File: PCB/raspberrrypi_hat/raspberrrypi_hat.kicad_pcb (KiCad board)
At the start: 4 copper layers, 65 x 56 mm, 18 parts, among them J3 40HAT, J6 CONN_02X02, J9 CONN_01X02, Q1 DMG2305UX, Q2 DMMT5401, U2 CAT24C32

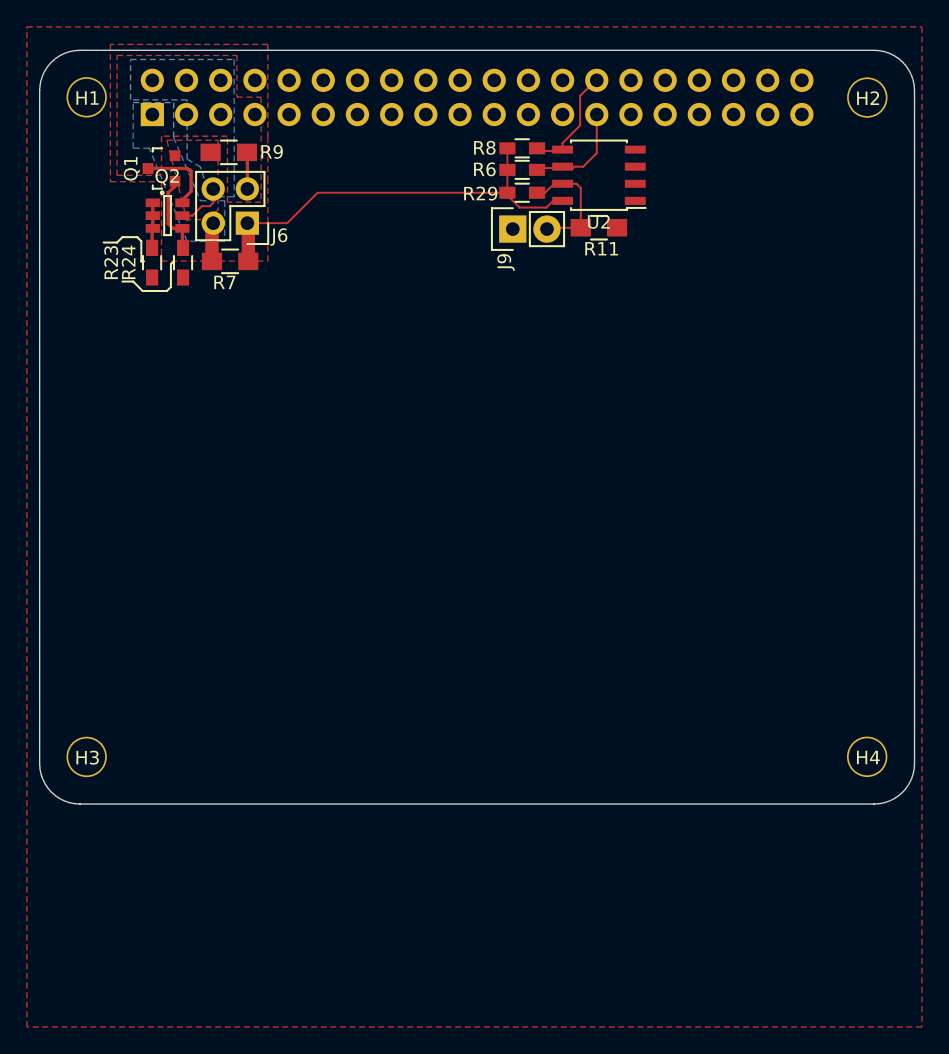
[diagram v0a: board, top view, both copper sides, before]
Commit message: Change Pi HAT footprints to SMD 1206_HandSoldering
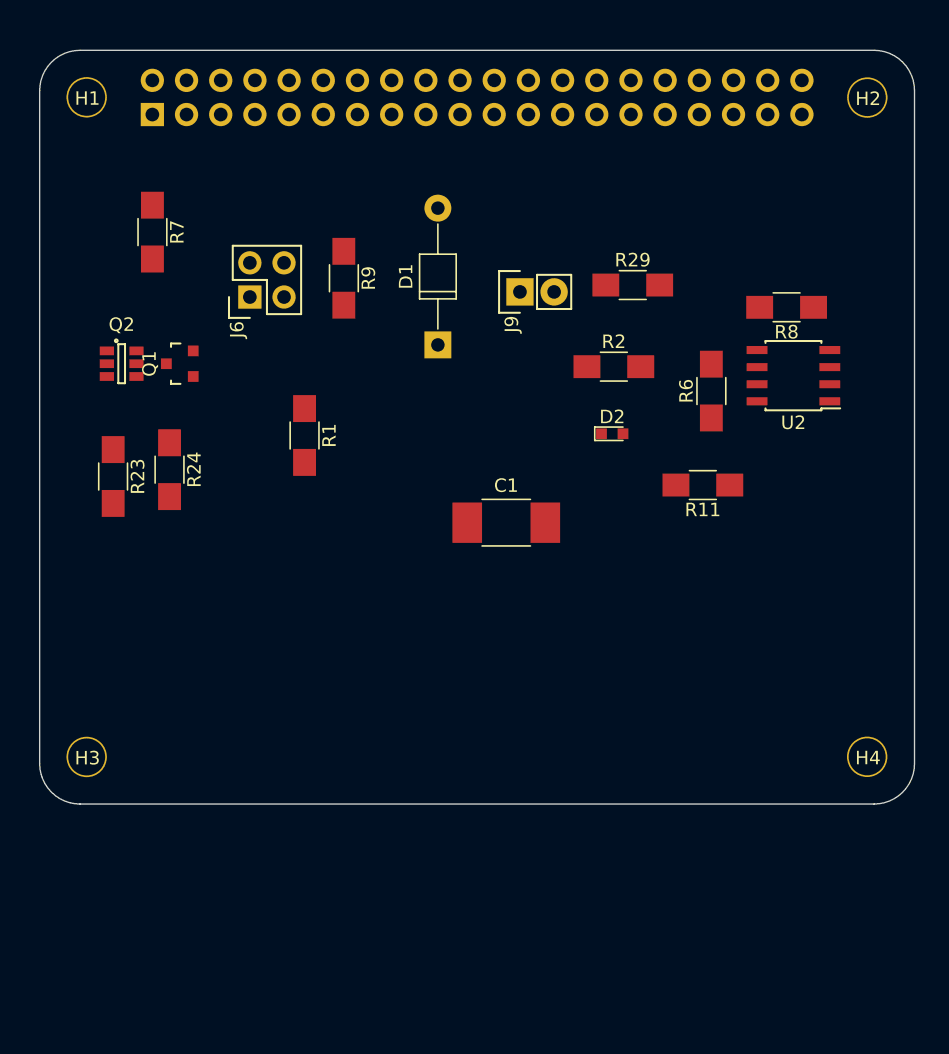
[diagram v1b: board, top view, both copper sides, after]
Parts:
- added C1: CP, Capacitors_SMD:C_1812_HandSoldering, F.Cu at (113.2, 95.9)
- added D1: D, Diodes_ThroughHole:D_T-1_P10.16mm_Horizontal, F.Cu at (108.1, 82.7)
- added D2: LED, LEDs:LED_0603, F.Cu at (121.1, 89.3)
- added R1: R, Resistors_SMD:R_1206_HandSoldering, F.Cu at (98.2, 89.4)
- added R2: R, Resistors_SMD:R_1206_HandSoldering, F.Cu at (121.2, 84.3)
- R11, R7, R9: footprint Resistors_SMD:R_0805_HandSoldering -> Resistors_SMD:R_1206_HandSoldering
- R23, R24, R29, R6, R8: footprint Resistors_SMD:R_0603_HandSoldering -> Resistors_SMD:R_1206_HandSoldering
- moved R8 22.9 mm to (134.0, 79.9), turned to 180 degrees
- moved R6 21.6 mm to (128.5, 86.1), turned to 90 degrees
- moved U2 20.7 mm to (134.6, 85.0)
- moved R11 20.6 mm to (127.8, 93.1), turned to 180 degrees
- moved R23 16.1 mm to (84.0, 92.5)
- moved R24 15.4 mm to (88.2, 92.0)
- moved Q1 14.6 mm to (89.0, 84.1)
- moved R9 12.7 mm to (101.1, 77.8), turned to 270 degrees
- moved Q2 11.5 mm to (84.6, 84.1)
- moved R29 10.7 mm to (122.6, 78.3)
- moved R7 6.17 mm to (86.9, 74.3), turned to 270 degrees
- moved J6 5.49 mm to (94.2, 79.1), turned to 90 degrees
- moved J9 4.70 mm to (114.2, 78.8)
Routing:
- net /P3V3: track 31.3 -> 0.00 mm
- net Net-(J9-Pad2): track 9.58 -> 0.00 mm
- net /P5V: track 9.02 -> 0.00 mm
- net /ID_SC_EEPROM: track 8.17 -> 0.11 mm
- net /ID_SD_EEPROM: track 8.99 -> 1.07 mm
- net Net-(Q1-Pad1): track 6.02 -> 0.00 mm
- net /P5V_HAT: track 3.77 -> 0.00 mm
- net Net-(Q2-Pad1): track 3.37 -> 0.00 mm
- net /P3V3_HAT: track 2.88 -> 0.00 mm
- removed copper zone on B.Cu, net /P3V3_HAT
- removed copper zone on F.Cu, net /P5V
- removed copper zone on B.Cu, net /P5V_HAT
- removed copper zone on F.Cu, net /P5V_HAT
- removed copper zone on F.Cu, net GND

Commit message: Connect hierarchical sheets
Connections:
- D1 pad 2: (no net) -> /P5V
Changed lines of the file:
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@@
 (kicad_pcb (version 4) (host pcbnew 4.0.6-e0-6349~53~ubuntu16.04.1)
   (general
-    (links 46)
-    (no_connects 38)
-    (area 78.496355 60.76761 143.596357 116.867612)
+    (links 47)
+    (no_connects 39)
+    (area 71.978573 45.025 229.685714 128.300001)
     (thickness 1.6)
     (drawings 54)
@@
     (mod_text_size 1 1)
     (mod_text_width 0.15)
-    (pad_size 1.524 1.524)
-    (pad_drill 0.762)
+    (pad_size 2 2)
+    (pad_drill 1)
     (pad_to_mask_clearance 0.2)
     (aux_axis_origin 0 0)
@@
     (pad 1 thru_hole rect (at 0 0 90) (size 2 2) (drill 1) (layers *.Cu *.Mask)
       (net 11 "Net-(C1-Pad1)"))
-    (pad 2 thru_hole oval (at 10.16 0 90) (size 2 2) (drill 1) (layers *.Cu *.Mask))
+    (pad 2 thru_hole oval (at 10.16 0 90) (size 2 2) (drill 1) (layers *.Cu *.Mask)
+      (net 9 /P5V))
     (model ${KISYS3DMOD}/Diodes_THT.3dshapes/D_T-1_P10.16mm_Horizontal.wrl
       (at (xyz 0 0 0))

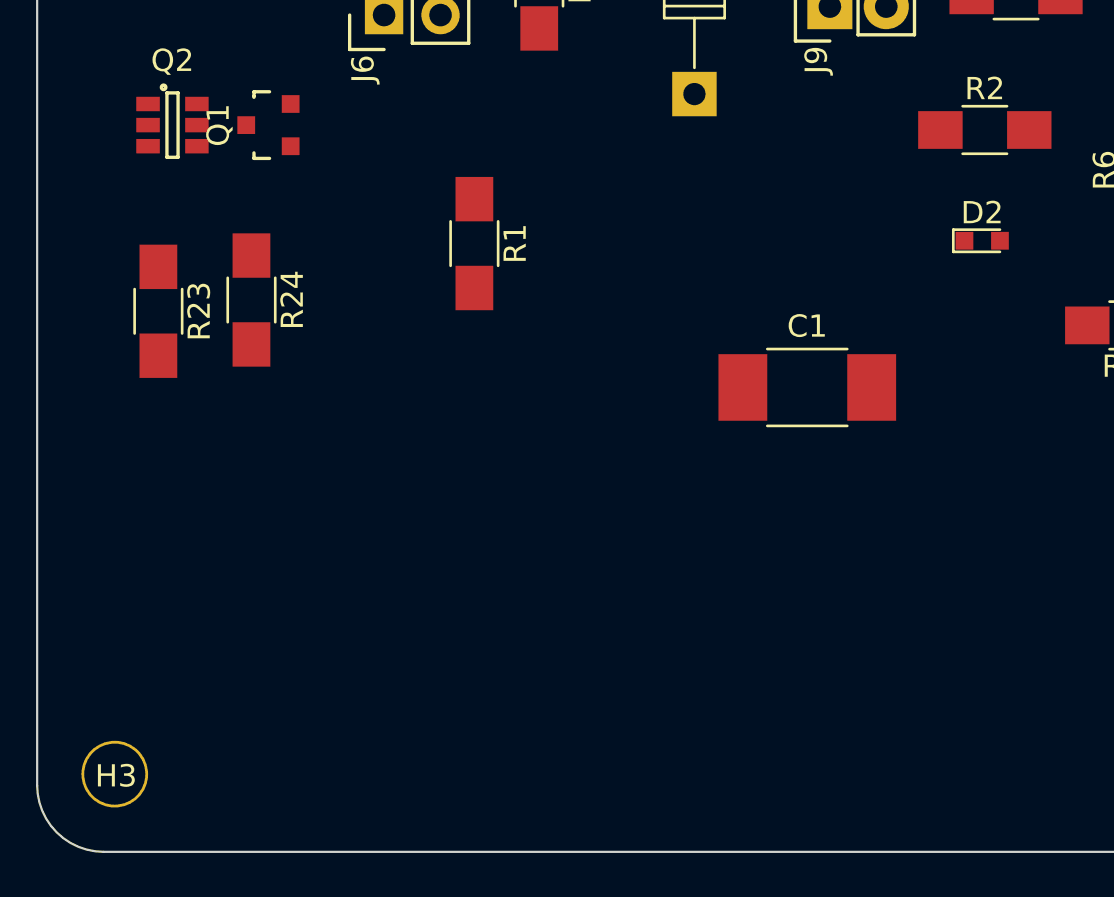
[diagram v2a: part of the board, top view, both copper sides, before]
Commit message: Create NeowayM590 footprint
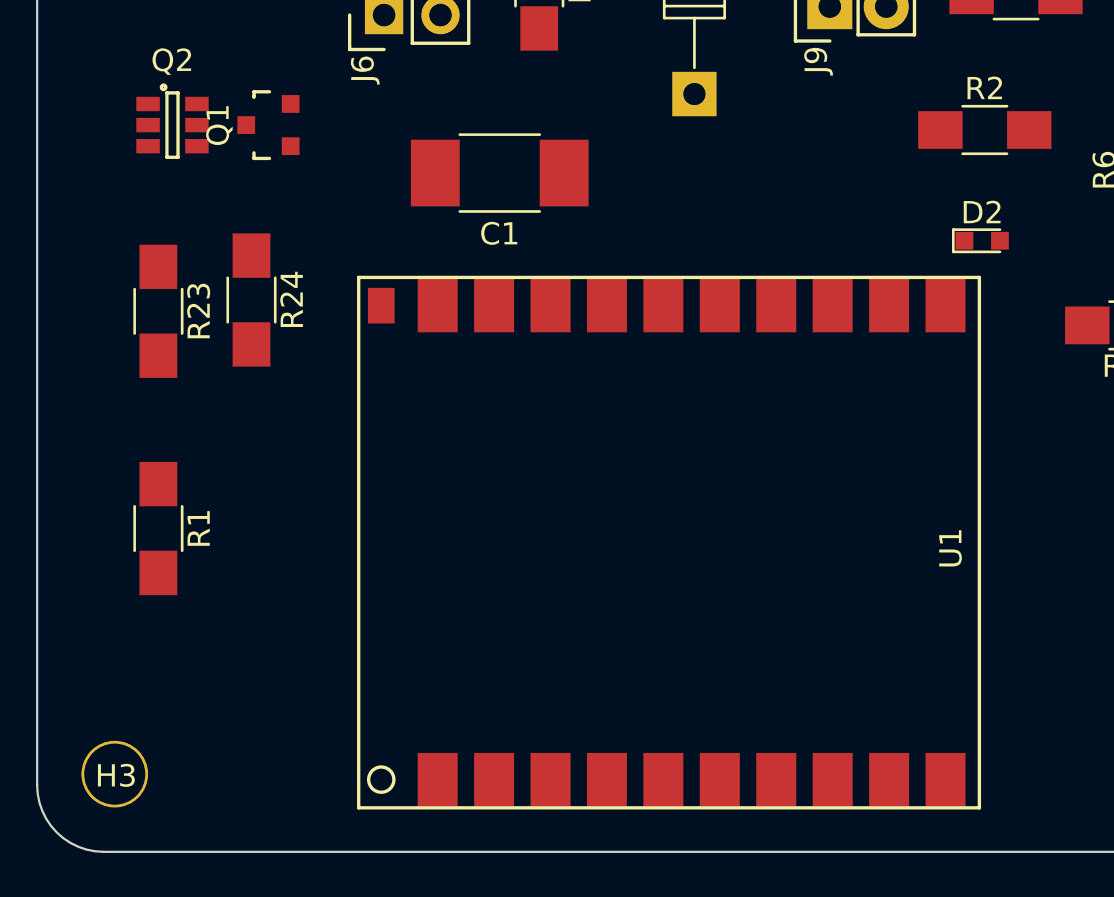
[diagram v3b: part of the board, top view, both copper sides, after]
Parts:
- added U1: NeowayM590, project_footprints:NeowayM590, F.Cu at (96.6, 113.6)
- moved R1 19.2 mm to (84.0, 102.3)
- moved C1 16.9 mm to (99.4, 86.3), turned to 180 degrees
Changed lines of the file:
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@@
 (kicad_pcb (version 4) (host pcbnew 4.0.6-e0-6349~53~ubuntu16.04.1)
   (general
-    (links 47)
-    (no_connects 39)
-    (area 71.978573 45.025 229.685714 128.300001)
+    (links 51)
+    (no_connects 43)
+    (area 78.496355 60.76761 143.596357 116.867612)
     (thickness 1.6)
     (drawings 54)
     (tracks 4)
     (zones 0)
-    (modules 23)
+    (modules 24)
     (nets 13)
   )
@@
   )
   (module Resistors_SMD:R_1206_HandSoldering (layer F.Cu)
-    (at 98.228 89.436 270)
+    (at 84.004 102.263 270)
     (descr "Resistor SMD 1206, hand soldering")
     (tags "resistor 1206")
@@
   )
   (module Capacitors_SMD:C_1812_HandSoldering (layer F.Cu)
-    (at 113.214 95.913)
+    (at 99.371 86.261 180)
     (descr "Capacitor SMD 1812, hand soldering")
     (tags "capacitor 1812")
     (attr smd)
-    (fp_text reference C1 (at 0 -2.75) (layer F.SilkS)
-      (effects (font (size 1 1) (thickness 0.15)))
-    )
-    (fp_text value CP (at 0 2.75) (layer F.Fab)
-      (effects (font (size 1 1) (thickness 0.15)))
-    )
-    (fp_text user %R (at 0 -2.75) (layer F.Fab)
+    (fp_text reference C1 (at 0 -2.75 180) (layer F.SilkS)
+      (effects (font (size 1 1) (thickness 0.15)))
+    )
+    (fp_text value CP (at 0 2.75 180) (layer F.Fab)
+      (effects (font (size 1 1) (thickness 0.15)))
+    )
+    (fp_text user %R (at 0 -2.75 180) (layer F.Fab)
       (effects (font (size 1 1) (thickness 0.15)))
     )
@@
     (fp_line (start 4.25 1.85) (end 4.25 -1.85) (layer F.CrtYd) (width 0.05))
     (fp_line (start 4.25 1.85) (end -4.25 1.85) (layer F.CrtYd) (width 0.05))
-    (pad 1 smd rect (at -2.9 0) (size 2.2 3) (layers F.Cu F.Paste F.Mask)
+    (pad 1 smd rect (at -2.9 0 180) (size 2.2 3) (layers F.Cu F.Paste F.Mask)
       (net 11 "Net-(C1-Pad1)"))
-    (pad 2 smd rect (at 2.9 0) (size 2.2 3) (layers F.Cu F.Paste F.Mask)
+    (pad 2 smd rect (at 2.9 0 180) (size 2.2 3) (layers F.Cu F.Paste F.Mask)
       (net 1 GND))
     (model Capacitors_SMD.3dshapes/C_1812.wrl
@@
     )
   )
+  (module project_footprints:NeowayM590 (layer F.Cu)
+    (at 96.577 113.566 90)
+    (fp_text reference U1 (at 10.414 23.114 90) (layer F.SilkS)
+      (effects (font (size 1 1) (thickness 0.15)))
+    )
+    (fp_text value NeowayM590 (at 11.176 9.144 90) (layer F.Fab)
+      (effects (font (size 1 1) (thickness 0.15)))
+    )
+    (fp_line (start -1.27 -3.556) (end 22.606 -3.556) (layer F.SilkS) (width 0.15))
+    (fp_line (start 22.606 -3.556) (end 22.606 24.384) (layer F.SilkS) (width 0.15))
+    (fp_line (start 22.606 24.384) (end -1.27 24.384) (layer F.SilkS) (width 0.15))
+    (fp_line (start -1.27 24.384) (end -1.27 -3.556) (layer F.SilkS) (width 0.15))
+    (fp_circle (center 0 -2.54) (end 0.508 -2.286) (layer F.SilkS) (width 0.15))
+    (fp_circle (center 0 -2.54) (end 0.508 -2.286) (layer F.Fab) (width 0.15))
+    (fp_line (start -1.27 -3.556) (end 22.606 -3.556) (layer F.Fab) (width 0.15))
+    (fp_line (start 22.606 -3.556) (end 22.606 24.384) (layer F.Fab) (width 0.15))
+    (fp_line (start 22.606 24.384) (end -1.27 24.384) (layer F.Fab) (width 0.15))
+    (fp_line (start -1.27 24.384) (end -1.27 -3.556) (layer F.Fab) (width 0.15))
+    (pad 14 smd rect (at 21.336 15.24 90) (size 2.4 1.8) (layers F.Cu F.Paste F.Mask))
+    (pad 1 smd rect (at 0 0 90) (size 2.4 1.8) (layers F.Cu F.Paste F.Mask)
+      (net 1 GND))
+    (pad 2 smd rect (at 0 2.54 90) (size 2.4 1.8) (layers F.Cu F.Paste F.Mask)
+      (net 9 /P5V))
+    (pad 3 smd rect (at 0 5.08 90) (size 2.4 1.8) (layers F.Cu F.Paste F.Mask)
+      (net 9 /P5V))
+    (pad 4 smd rect (at 0 7.62 90) (size 2.4 1.8) (layers F.Cu F.Paste F.Mask))
+    (pad 5 smd rect (at 0 10.16 90) (size 2.4 1.8) (layers F.Cu F.Paste F.Mask))
+    (pad 6 smd rect (at 0 12.7 90) (size 2.4 1.8) (layers F.Cu F.Paste F.Mask))
+    (pad 7 smd rect (at 0 15.24 90) (size 2.4 1.8) (layers F.Cu F.Paste F.Mask))
+    (pad 8 smd rect (at 0 17.78 90) (size 2.4 1.8) (layers F.Cu F.Paste F.Mask))
+    (pad 9 smd rect (at 0 20.32 90) (size 2.4 1.8) (layers F.Cu F.Paste F.Mask))
+    (pad 10 smd rect (at 0 22.86 90) (size 2.4 1.8) (layers F.Cu F.Paste F.Mask))
+    (pad 11 smd rect (at 21.336 22.86 90) (size 2.4 1.8) (layers F.Cu F.Paste F.Mask))
+    (pad 12 smd rect (at 21.336 20.32 90) (size 2.4 1.8) (layers F.Cu F.Paste F.Mask))
+    (pad 13 smd rect (at 21.336 17.78 90) (size 2.4 1.8) (layers F.Cu F.Paste F.Mask))
+    (pad 15 smd rect (at 21.336 12.7 90) (size 2.4 1.8) (layers F.Cu F.Paste F.Mask))
+    (pad 16 smd rect (at 21.336 10.16 90) (size 2.4 1.8) (layers F.Cu F.Paste F.Mask))
+    (pad 17 smd rect (at 21.336 7.62 90) (size 2.4 1.8) (layers F.Cu F.Paste F.Mask))
+    (pad 18 smd rect (at 21.336 5.08 90) (size 2.4 1.8) (layers F.Cu F.Paste F.Mask))
+    (pad 19 smd rect (at 21.336 2.54 90) (size 2.4 1.8) (layers F.Cu F.Paste F.Mask))
+    (pad 20 smd rect (at 21.336 0 90) (size 2.4 1.8) (layers F.Cu F.Paste F.Mask)
+      (net 1 GND))
+    (pad 21 smd rect (at 21.336 -2.54 90) (size 1.6 1.2) (layers F.Cu F.Paste F.Mask))
+  )
   (gr_text "If you want to use an SMT 40-pin header, please move the top edge up \nby 0.5mm and locate the header in the same location as the current TH part." (at 117.3 47.5) (layer Cmts.User)
